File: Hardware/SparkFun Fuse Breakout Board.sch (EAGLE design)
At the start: 9 parts, among them J2 POWER_JACKPTH_LOCK

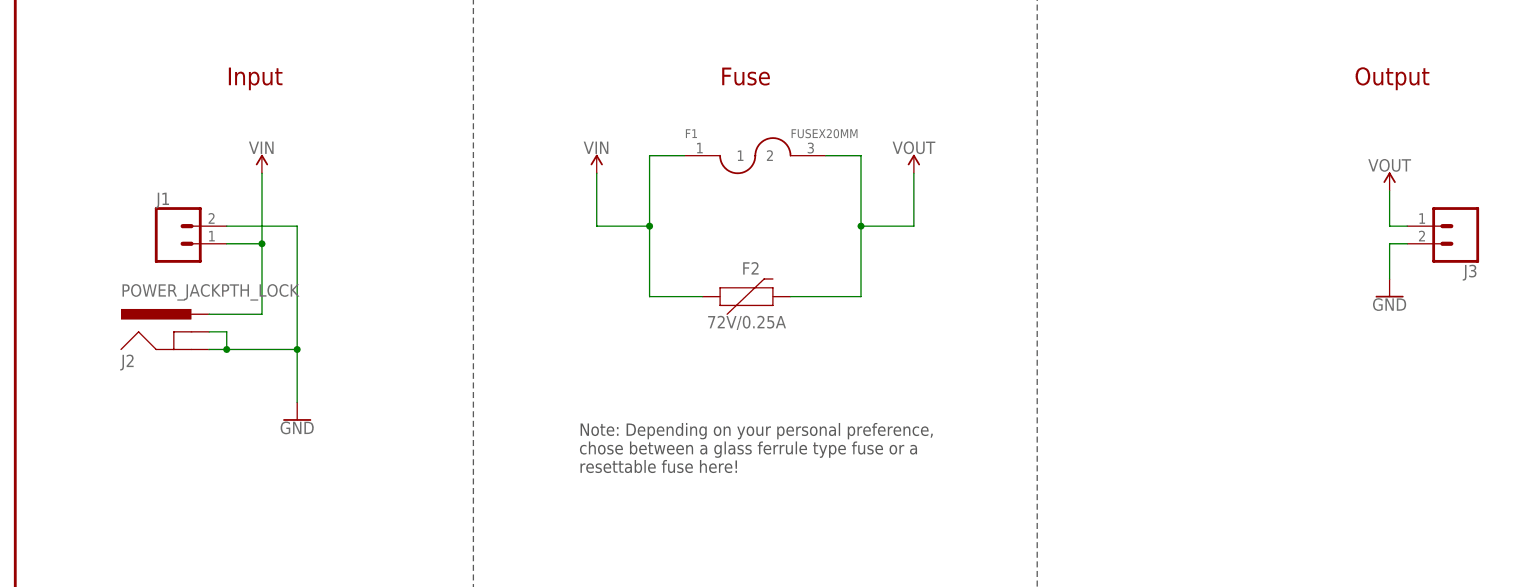
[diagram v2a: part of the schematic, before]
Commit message: Update Note in Schematic
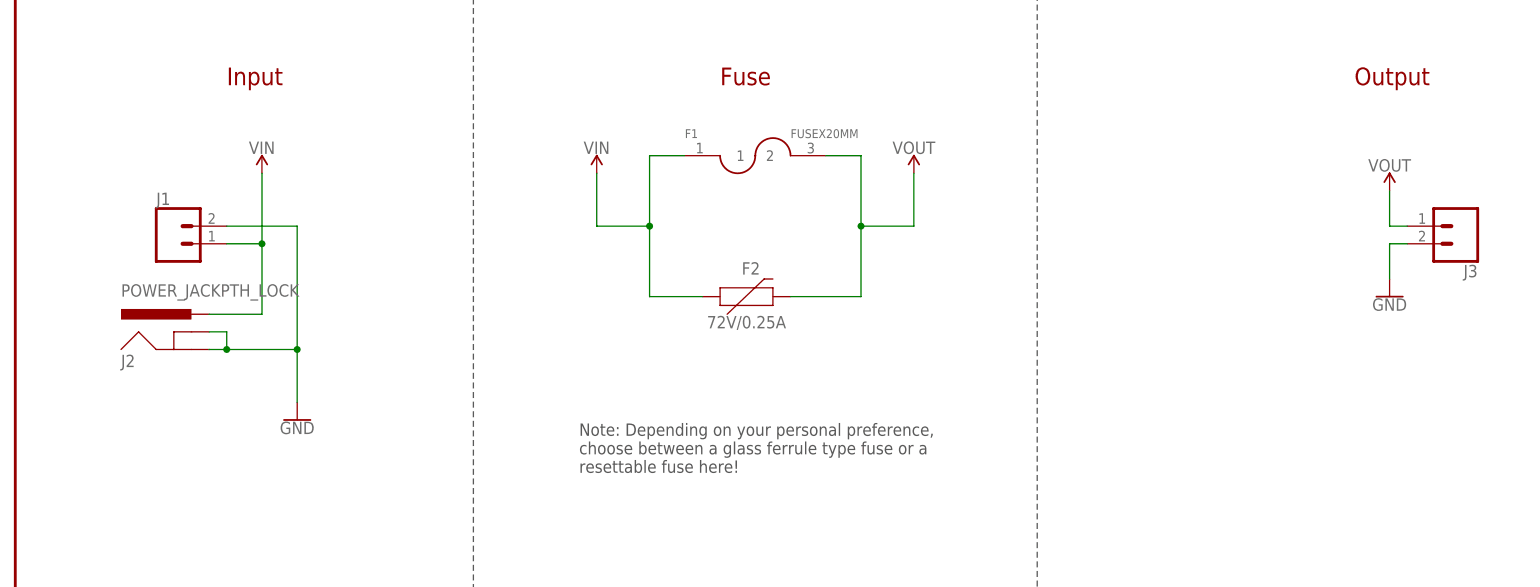
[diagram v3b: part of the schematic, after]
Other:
- note added: "Note: Depending on your personal preference, choose between a glass ferrule type fuse or a resettable fuse here!"
- note removed: "Note: Depending on your personal preference, chose between a glass ferrule type fuse or a resettable fuse here!"
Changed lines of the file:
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@@
 <?xml version="1.0" encoding="utf-8"?>
 <!DOCTYPE eagle SYSTEM "eagle.dtd">
-<eagle version="8.5.2">
+<eagle version="9.5.0">
 <drawing>
 <settings>
@@
 <text x="237.744" y="6.604" size="3.81" layer="97" font="vector" ratio="15">v1.0</text>
 <text x="81.28" y="83.82" size="1.778" layer="97" font="vector" ratio="15">Note: Depending on your personal preference,
-chose between a glass ferrule type fuse or a
+choose between a glass ferrule type fuse or a
 resettable fuse here!</text>
 </plain>
 <instances>
-<instance part="FRAME1" gate="G$1" x="0" y="0"/>
-<instance part="FRAME1" gate="V" x="147.32" y="0"/>
-<instance part="F1" gate="G$1" x="106.68" y="129.54"/>
-<instance part="GND1" gate="1" x="40.64" y="91.44"/>
-<instance part="F2" gate="F1" x="104.14" y="109.22"/>
-<instance part="GND3" gate="1" x="198.12" y="109.22"/>
-<instance part="SUPPLY2" gate="G$1" x="198.12" y="124.46"/>
-<instance part="SUPPLY1" gate="G$1" x="35.56" y="127"/>
-<instance part="SUPPLY3" gate="G$1" x="83.82" y="127"/>
-<instance part="SUPPLY4" gate="G$1" x="129.54" y="127"/>
-<instance part="LOGO1" gate="G$1" x="190.5" y="35.56"/>
-<instance part="LOGO2" gate="G$1" x="177.8" y="38.1"/>
-<instance part="LOGO3" gate="G$1" x="160.02" y="45.72"/>
-<instance part="J2" gate="G$1" x="25.4" y="99.06"/>
-<instance part="J1" gate="G$1" x="22.86" y="116.84"/>
-<instance part="J3" gate="G$1" x="208.28" y="119.38" rot="R180"/>
+<instance part="FRAME1" gate="G$1" x="0" y="0" smashed="yes"/>
+<instance part="FRAME1" gate="V" x="147.32" y="0" smashed="yes">
+<attribute name="LAST_DATE_TIME" x="160.02" y="1.27" size="2.54" layer="94" font="vector"/>
+<attribute name="SHEET" x="233.68" y="1.27" size="2.54" layer="94" font="vector"/>
+<attribute name="DRAWING_NAME" x="162.814" y="17.78" size="2.7432" layer="94" font="vector"/>
+<attribute name="DESIGNER" x="170.434" y="11.176" size="2.7432" layer="94" font="vector"/>
+<attribute name="REV" x="236.22" y="6.604" size="2.7432" layer="94" font="vector"/>
+</instance>
+<instance part="F1" gate="G$1" x="106.68" y="129.54" smashed="yes">
+<attribute name="NAME" x="96.52" y="132.08" size="1.27" layer="95"/>
+<attribute name="VALUE" x="111.76" y="132.08" size="1.27" layer="96"/>
+</instance>
+<instance part="GND1" gate="1" x="40.64" y="91.44" smashed="yes">
+<attribute name="VALUE" x="40.64" y="91.186" size="1.778" layer="96" align="top-center"/>
+</instance>
+<instance part="F2" gate="F1" x="104.14" y="109.22" smashed="yes">
+<attribute name="NAME" x="106.045" y="112.395" size="1.778" layer="95" font="vector" align="bottom-center"/>
+<attribute name="VALUE" x="105.41" y="106.426" size="1.778" layer="96" font="vector" align="top-center"/>
+</instance>
+<instance part="GND3" gate="1" x="198.12" y="109.22" smashed="yes">
+<attribute name="VALUE" x="198.12" y="108.966" size="1.778" layer="96" align="top-center"/>
+</instance>
+<instance part="SUPPLY2" gate="G$1" x="198.12" y="124.46" smashed="yes">
+<attribute name="VALUE" x="198.12" y="127.254" size="1.778" layer="96" align="bottom-center"/>
+</instance>
+<instance part="SUPPLY1" gate="G$1" x="35.56" y="127" smashed="yes">
+<attribute name="VALUE" x="35.56" y="129.794" size="1.778" layer="96" align="bottom-center"/>
+</instance>
+<instance part="SUPPLY3" gate="G$1" x="83.82" y="127" smashed="yes">
+<attribute name="VALUE" x="83.82" y="129.794" size="1.778" layer="96" align="bottom-center"/>
+</instance>
+<instance part="SUPPLY4" gate="G$1" x="129.54" y="127" smashed="yes">
+<attribute name="VALUE" x="129.54" y="129.794" size="1.778" layer="96" align="bottom-center"/>
+</instance>
+<instance part="LOGO1" gate="G$1" x="190.5" y="35.56" smashed="yes"/>
+<instance part="LOGO2" gate="G$1" x="177.8" y="38.1" smashed="yes"/>
+<instance part="LOGO3" gate="G$1" x="160.02" y="45.72" smashed="yes"/>
+<instance part="J2" gate="G$1" x="25.4" y="99.06" smashed="yes">
+<attribute name="VALUE" x="15.24" y="109.22" size="1.778" layer="96" font="vector"/>
+<attribute name="NAME" x="15.24" y="99.06" size="1.778" layer="95" font="vector"/>
+</instance>
+<instance part="J1" gate="G$1" x="22.86" y="116.84" smashed="yes">
+<attribute name="VALUE" x="20.32" y="112.014" size="1.778" layer="96" font="vector"/>
+<attribute name="NAME" x="20.32" y="122.428" size="1.778" layer="95" font="vector"/>
+</instance>
+<instance part="J3" gate="G$1" x="208.28" y="119.38" smashed="yes" rot="R180">
+<attribute name="VALUE" x="210.82" y="124.206" size="1.778" layer="96" font="vector" rot="R180"/>
+<attribute name="NAME" x="210.82" y="113.792" size="1.778" layer="95" font="vector" rot="R180"/>
+</instance>
 </instances>
 <busses>
